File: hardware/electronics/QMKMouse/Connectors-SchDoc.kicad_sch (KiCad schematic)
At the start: 19 parts

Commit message: small fix
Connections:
- net GND: now also USB.C.19.1; no longer USB.C.19.2
- net V_USB: now also USB.C.19.2; no longer USB.C.19.1
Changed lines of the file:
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@@
     (pin "2")
   )
-  (symbol (lib_id "Device:C") (at 218.44 93.98 0) (unit 1)
+  (symbol (lib_id "Device:C") (at 218.44 93.98 0) (mirror x) (unit 1)
     (in_bom yes) (on_board yes) (fields_autoplaced)
-    (property "Reference" "USB.C.19" (id 0) (at 222.25 92.7099 0)
-      (effects (font (size 1.27 1.27)) (justify left))
+    (property "Reference" "USB.C.19" (id 0) (at 214.63 92.7099 0)
+      (effects (font (size 1.27 1.27)) (justify right))
     )
-    (property "Value" "10uF 25V" (id 1) (at 222.25 95.2499 0)
-      (effects (font (size 1.27 1.27)) (justify left))
+    (property "Value" "10uF 25V" (id 1) (at 214.63 95.2499 0)
+      (effects (font (size 1.27 1.27)) (justify right))
     )
-    (property "Footprint" "" (id 2) (at 219.4052 97.79 0)
+    (property "Footprint" "" (id 2) (at 219.4052 90.17 0)
       (effects (font (size 1.27 1.27)) hide)
     )

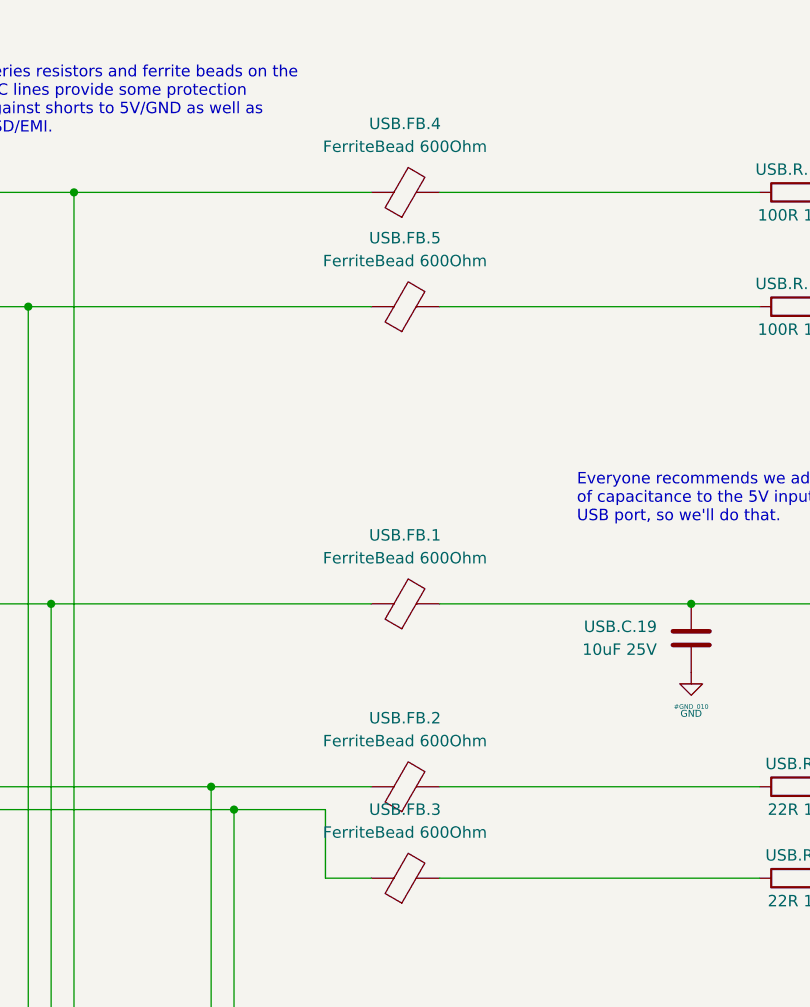
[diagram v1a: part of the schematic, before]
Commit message: update schematic components
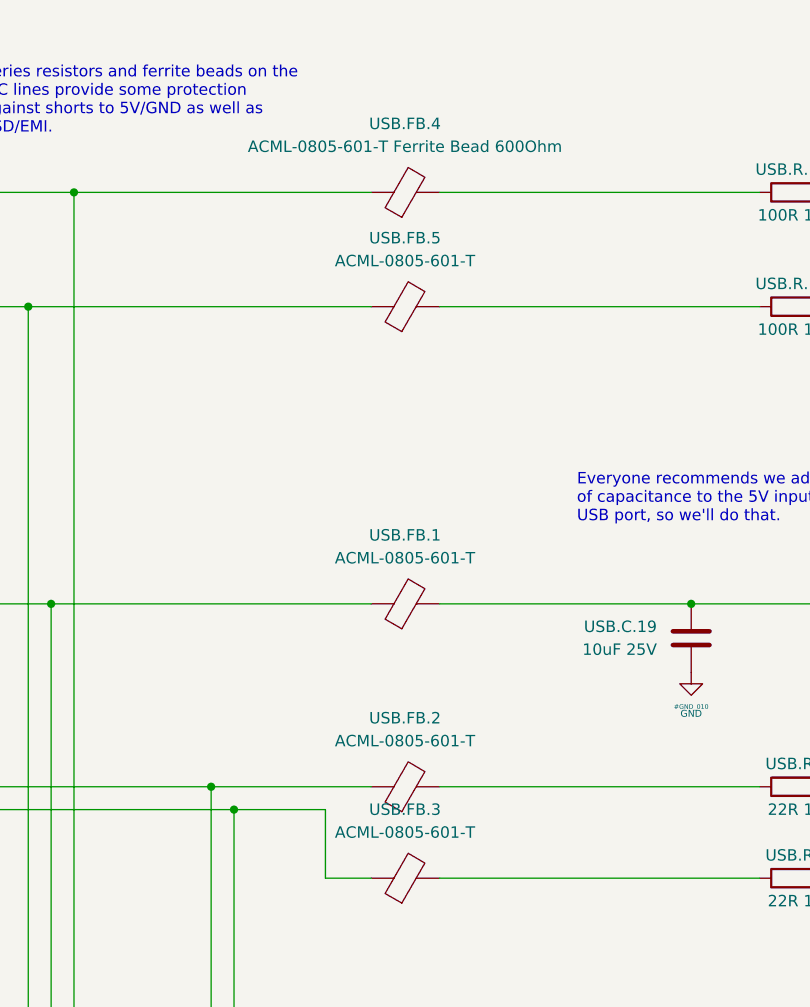
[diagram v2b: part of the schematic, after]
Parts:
- USB.FB.1, USB.FB.2, USB.FB.3, USB.FB.5: value FerriteBead 600Ohm -> ACML-0805-601-T
- USB.FB.4: value FerriteBead 600Ohm -> ACML-0805-601-T Ferrite Bead 600Ohm
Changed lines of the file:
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@@
     (in_bom yes) (on_board yes) (fields_autoplaced)
     (property "Reference" "USB.FB.1" (id 0) (at 186.6392 82.55 90))
-    (property "Value" "FerriteBead 600Ohm" (id 1) (at 186.6392 85.09 90))
+    (property "Value" "ACML-0805-601-T" (id 1) (at 186.6392 85.09 90))
     (property "Footprint" "" (id 2) (at 186.69 91.948 90)
       (effects (font (size 1.27 1.27)) hide)
@@
     (in_bom yes) (on_board yes) (fields_autoplaced)
     (property "Reference" "USB.FB.5" (id 0) (at 186.6392 49.53 90))
-    (property "Value" "FerriteBead 600Ohm" (id 1) (at 186.6392 52.07 90))
+    (property "Value" "ACML-0805-601-T" (id 1) (at 186.6392 52.07 90))
     (property "Footprint" "" (id 2) (at 186.69 58.928 90)
       (effects (font (size 1.27 1.27)) hide)
@@
     (in_bom yes) (on_board yes) (fields_autoplaced)
     (property "Reference" "USB.FB.2" (id 0) (at 186.6392 102.87 90))
-    (property "Value" "FerriteBead 600Ohm" (id 1) (at 186.6392 105.41 90))
+    (property "Value" "ACML-0805-601-T" (id 1) (at 186.6392 105.41 90))
     (property "Footprint" "" (id 2) (at 186.69 112.268 90)
       (effects (font (size 1.27 1.27)) hide)
@@
     (in_bom yes) (on_board yes) (fields_autoplaced)
     (property "Reference" "USB.FB.4" (id 0) (at 186.6392 36.83 90))
-    (property "Value" "FerriteBead 600Ohm" (id 1) (at 186.6392 39.37 90))
+    (property "Value" "ACML-0805-601-T Ferrite Bead 600Ohm" (id 1) (at 186.6392 39.37 90))
     (property "Footprint" "" (id 2) (at 186.69 46.228 90)
       (effects (font (size 1.27 1.27)) hide)
@@
     (in_bom yes) (on_board yes) (fields_autoplaced)
     (property "Reference" "USB.FB.3" (id 0) (at 186.6392 113.03 90))
-    (property "Value" "FerriteBead 600Ohm" (id 1) (at 186.6392 115.57 90))
+    (property "Value" "ACML-0805-601-T" (id 1) (at 186.6392 115.57 90))
     (property "Footprint" "" (id 2) (at 186.69 122.428 90)
       (effects (font (size 1.27 1.27)) hide)
